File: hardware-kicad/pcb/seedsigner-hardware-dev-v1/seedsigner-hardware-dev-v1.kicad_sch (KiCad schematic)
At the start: 17 parts, among them U1 LuckFox_Pico_MINI, U2 WAVESHARE_LCD_BUTTON_BOARD_1.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

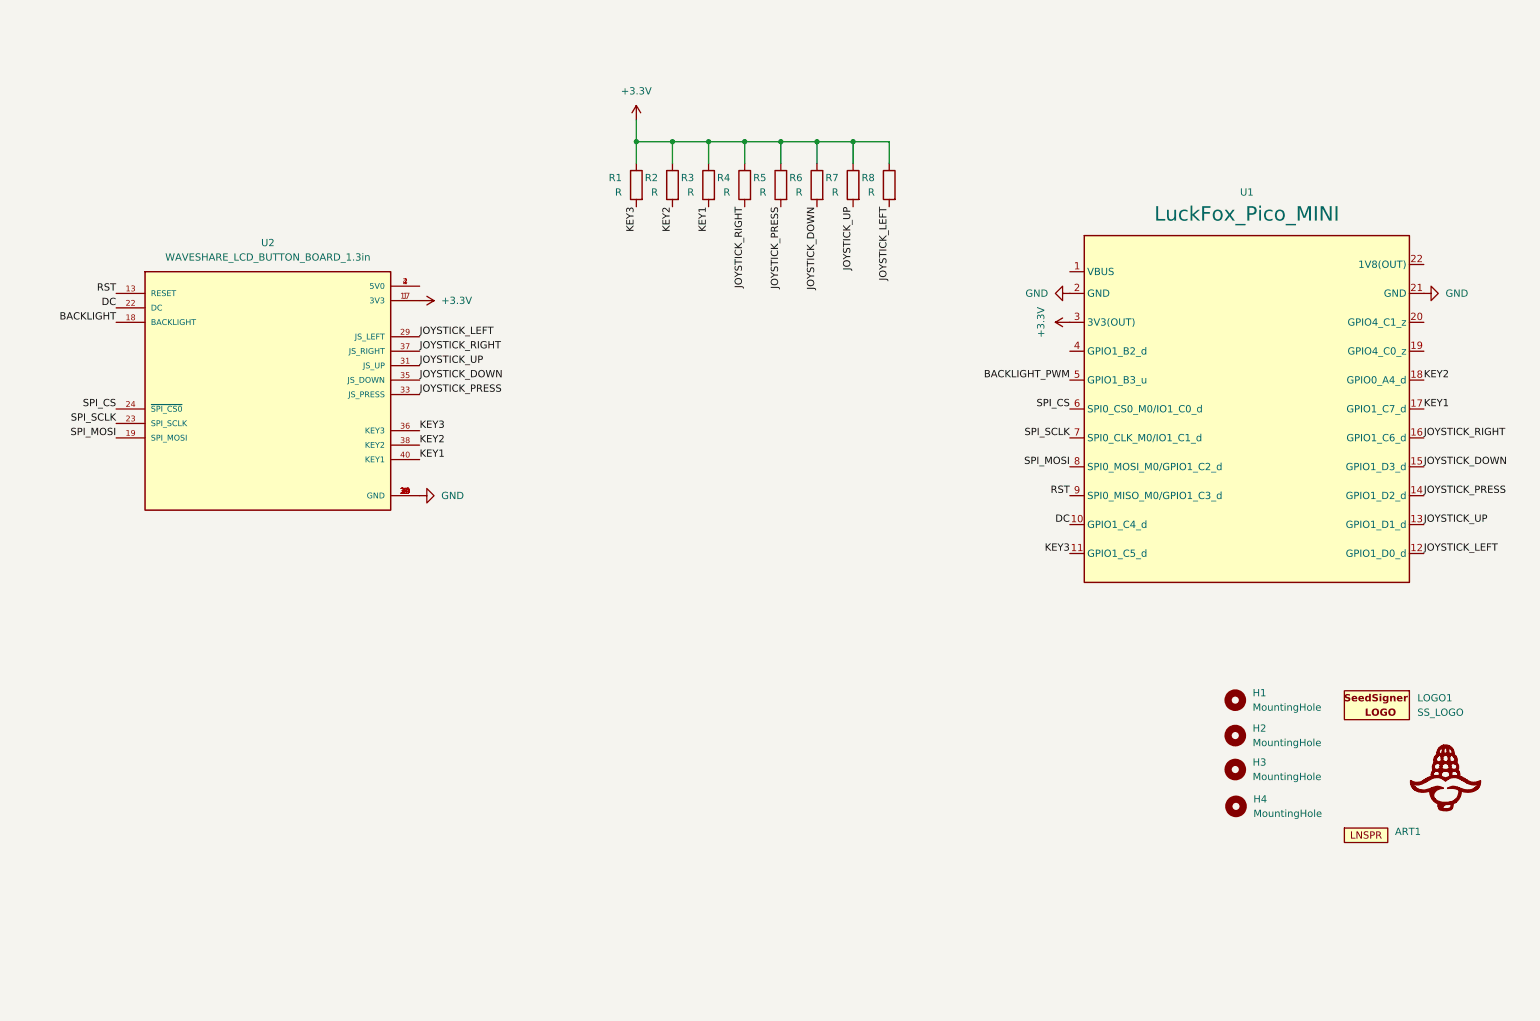
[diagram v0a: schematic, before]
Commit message: seedsigner hardware dev v1 all footprints created and placed
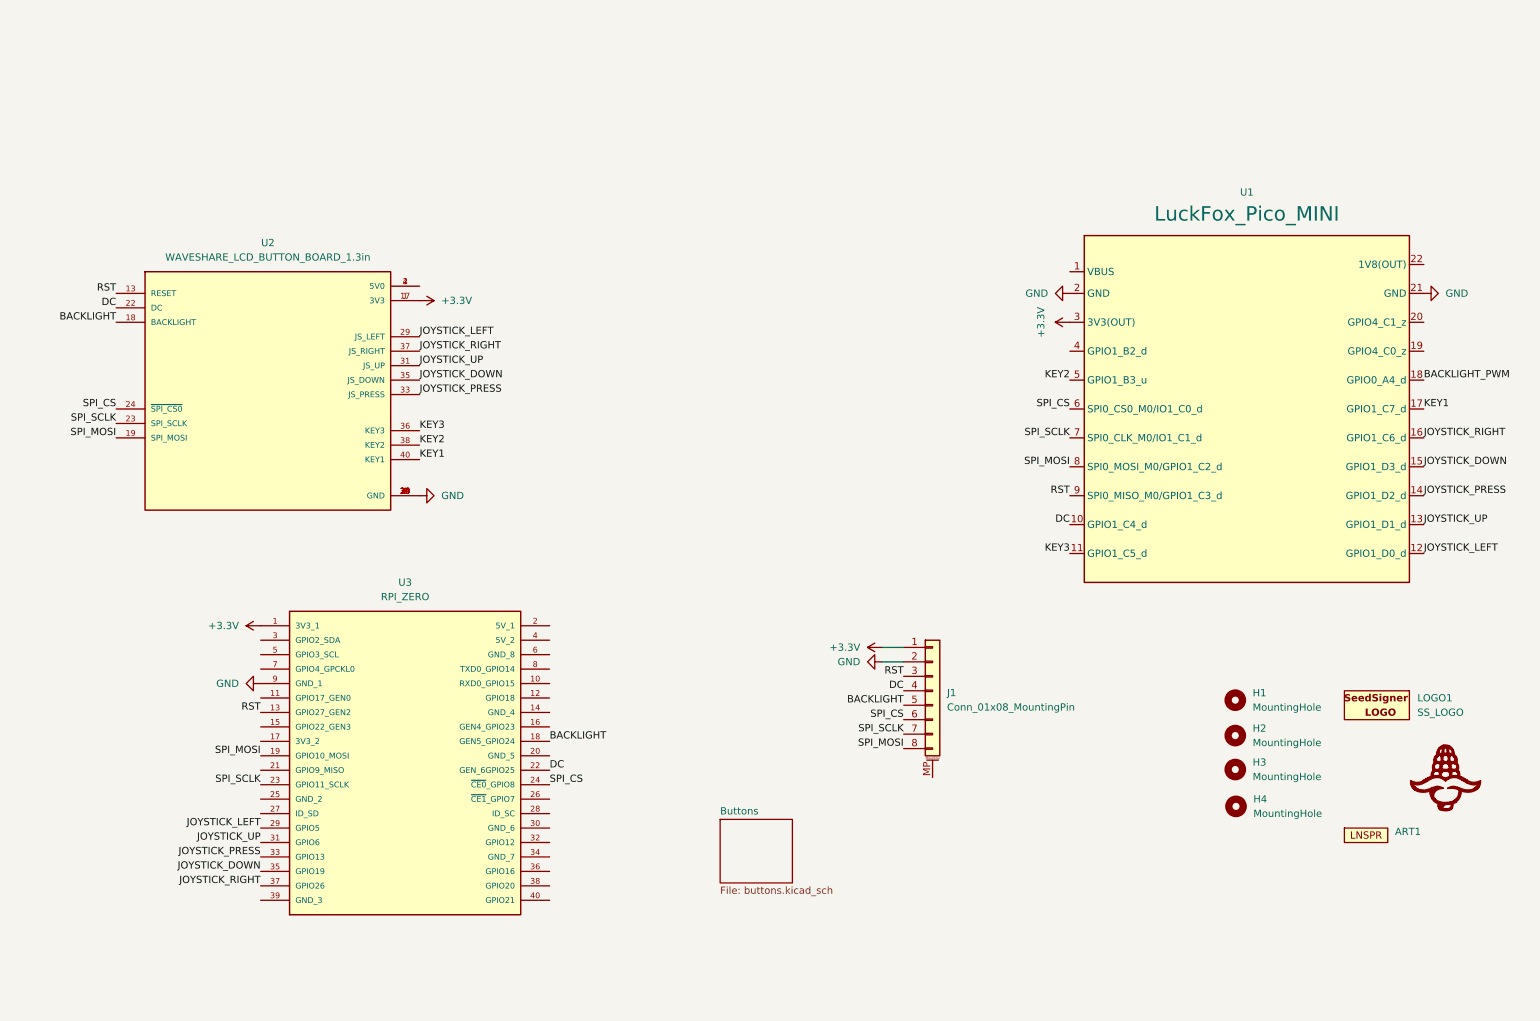
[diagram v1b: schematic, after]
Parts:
- removed R1, R2, R3, R4, R5, R6, R7, R8: R, Resistor_SMD:R_0603_1608Metric_Pad0.98x0.95mm_HandSolder, symbol Device:R
- added J1: Conn_01x08_MountingPin, Connector_PinHeader_2.54mm:PinHeader_1x08_P2.54mm_Horizontal, symbol Connector_Generic_MountingPin:Conn_01x08_MountingPin
- added U3: RPI_ZERO, seedsigner-luckfox:RPi_Zero, symbol SeedSigner:RPI_ZERO
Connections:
- net +3.3V: now also J1.1 (Pin_1), U3.1 (3V3_1)
- net BACKLIGHT: now also J1.5 (Pin_5), U3.18 (GEN5_GPIO24)
- net BACKLIGHT_PWM: now also U1.18 (GPIO0_A4_d); no longer U1.5 (GPIO1_B3_u)
- net DC: now also J1.4 (Pin_4), U3.22 (GEN_6GPIO25)
- net GND: now also J1.2 (Pin_2), U3.9 (GND_1)
- net JOYSTICK_DOWN: now also U3.35 (GPIO19)
- net JOYSTICK_LEFT: now also U3.29 (GPIO5)
- net JOYSTICK_PRESS: now also U3.33 (GPIO13)
- net JOYSTICK_RIGHT: now also U3.37 (GPIO26)
- net JOYSTICK_UP: now also U3.31 (GPIO6)
- net KEY2: now also U1.5 (GPIO1_B3_u); no longer U1.18 (GPIO0_A4_d)
- net RST: now also J1.3 (Pin_3), U3.13 (GPIO27_GEN2)
- net SPI_CS: now also J1.6 (Pin_6), U3.24 (~{CE0}_GPIO8)
- net SPI_MOSI: now also J1.8 (Pin_8), U3.19 (GPIO10_MOSI)
- net SPI_SCLK: now also J1.7 (Pin_7), U3.23 (GPIO11_SCLK)
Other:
- added sheet Buttons (buttons.kicad_sch)

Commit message: use hierarchical sheets in kicad
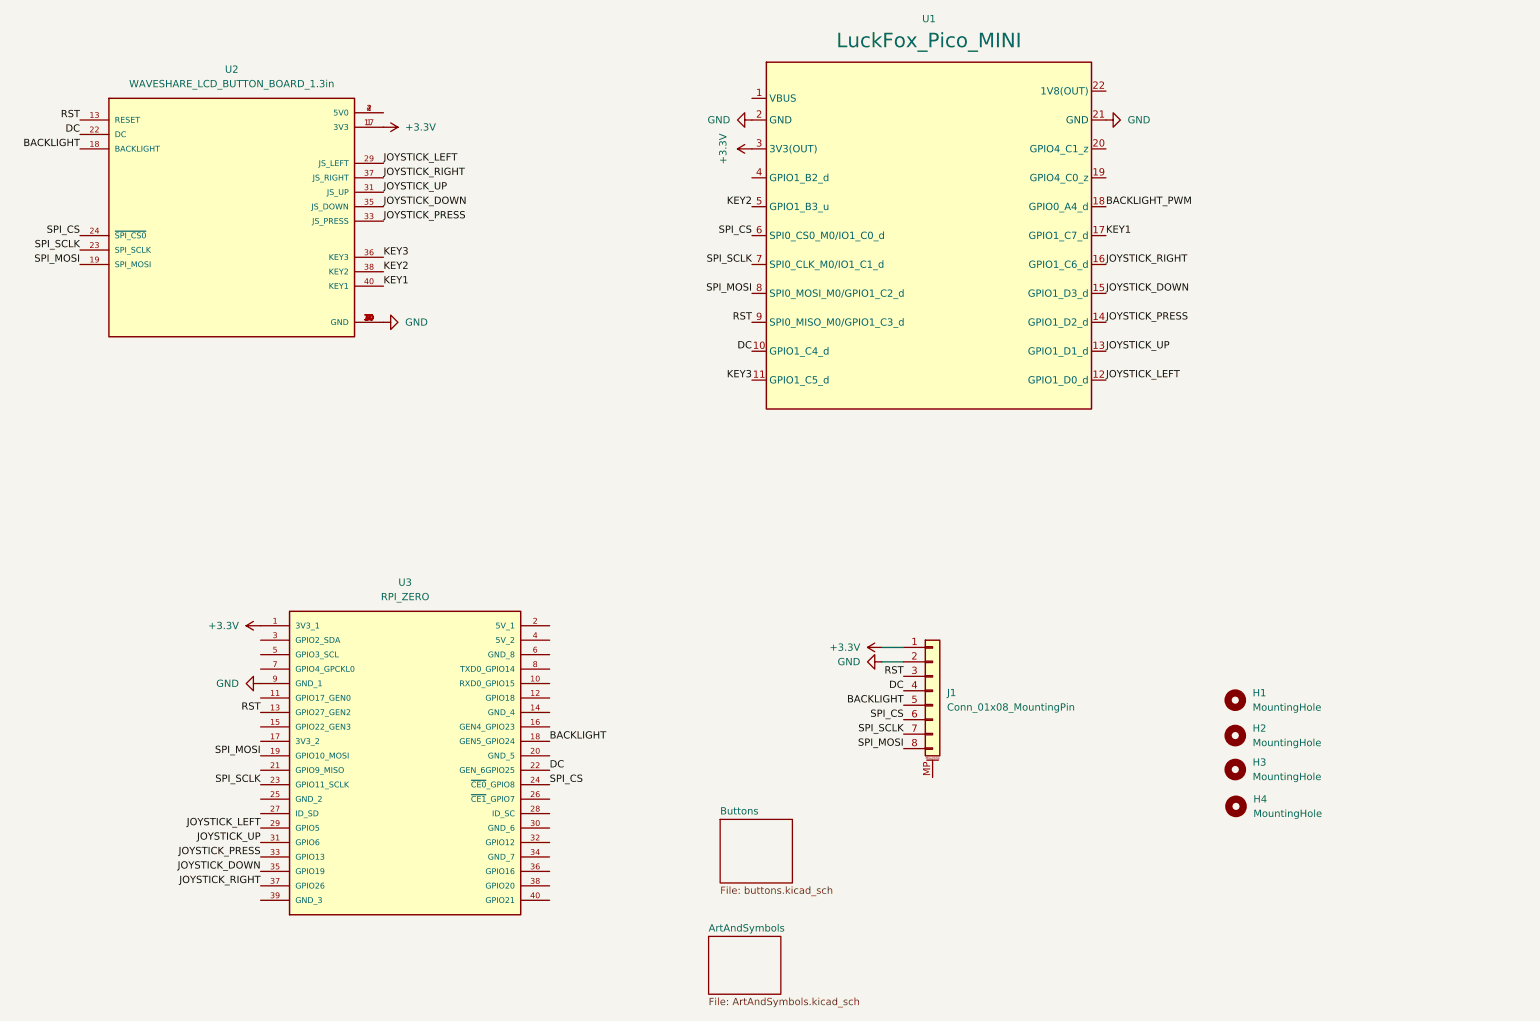
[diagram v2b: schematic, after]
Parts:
- removed ART1: ~, seedsigner-luckfox:LightningSpore_Logo, symbol seedsigner:LIGHTNINGSPORE
- removed LOGO1: SS_LOGO, seedsigner-luckfox:seedsigner-logo-small, symbol SeedSigner:SS_LOGO
- removed LOGO2: CORN-LOGO, seedsigner-luckfox:corn-logo, symbol SeedSigner:CORN-LOGO
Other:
- added sheet ArtAndSymbols (ArtAndSymbols.kicad_sch)
- moved on the sheet: U1, U2

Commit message: update library paths and modularize sch
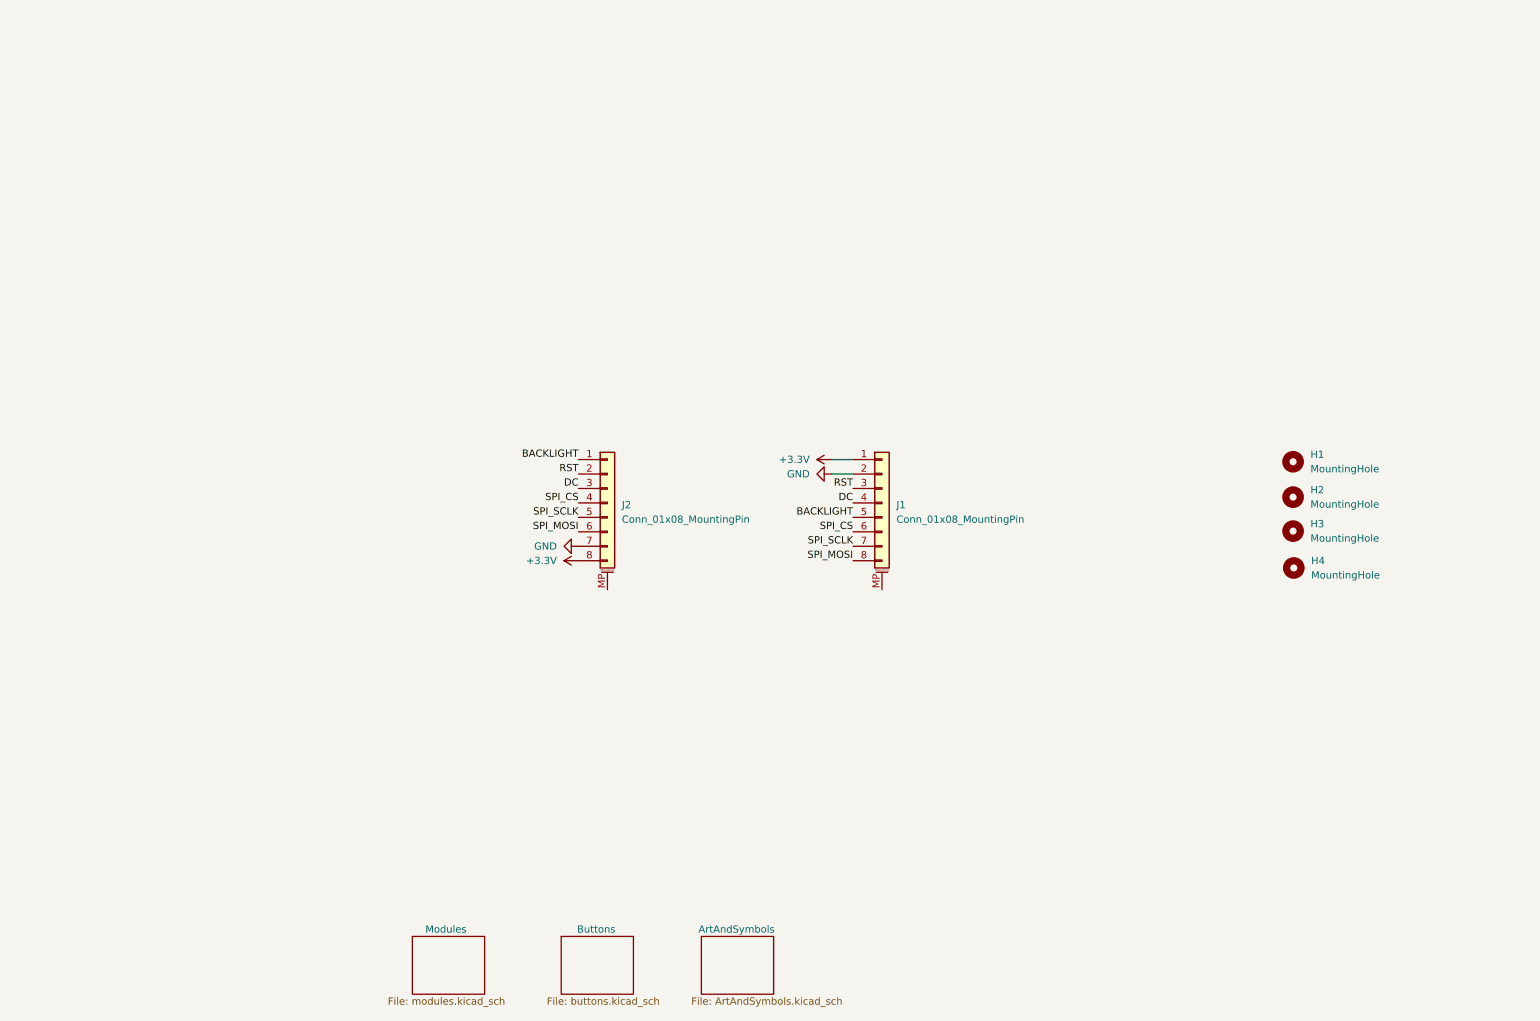
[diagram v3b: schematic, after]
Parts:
- removed U1: LuckFox_Pico_MINI, seedsigner-luckfox:LUCKFOX_PICO_MINI, symbol Luckfox:LuckFox_Pico_MINI
- removed U2: WAVESHARE_LCD_BUTTON_BOARD_1.3in, seedsigner-luckfox:WAVESHARE_LCD_BUTTON, symbol SeedSigner:WAVESHARE_LCD_BUTTON
- removed U3: RPI_ZERO, seedsigner-luckfox:RPi_Zero, symbol SeedSigner:RPI_ZERO
- added J2: Conn_01x08_MountingPin, Connector_PinHeader_2.54mm:PinHeader_1x08_P2.54mm_Horizontal, symbol Connector_Generic_MountingPin:Conn_01x08_MountingPin
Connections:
- net +3.3V: now also J2.8 (Pin_8)
- net BACKLIGHT: now also J2.1 (Pin_1)
- net DC: now also J2.3 (Pin_3)
- net GND: now also J2.7 (Pin_7)
- net RST: now also J2.2 (Pin_2)
- net SPI_CS: now also J2.4 (Pin_4)
- net SPI_MOSI: now also J2.6 (Pin_6)
- net SPI_SCLK: now also J2.5 (Pin_5)
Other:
- added sheet Modules (modules.kicad_sch)
- moved on the sheet: H1, H2, H3, H4, J1

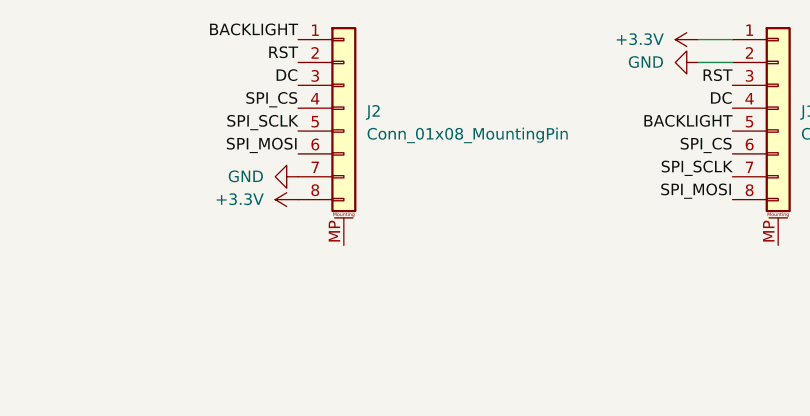
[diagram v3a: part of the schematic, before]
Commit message: autoroute the hardware devboard
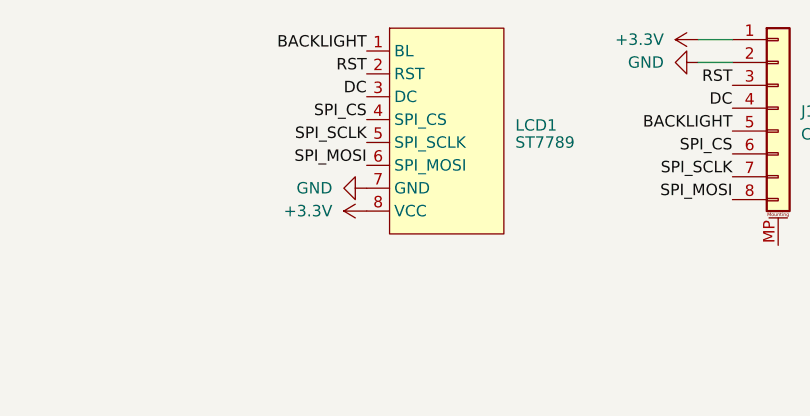
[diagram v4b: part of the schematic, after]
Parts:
- removed J2: Conn_01x08_MountingPin, Connector_PinHeader_2.54mm:PinHeader_1x08_P2.54mm_Horizontal, symbol Connector_Generic_MountingPin:Conn_01x08_MountingPin
- added LCD1: ST7789, Connector_PinHeader_2.54mm:PinHeader_1x08_P2.54mm_Vertical, symbol SeedSigner:LCD_ST7789
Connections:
- net +3.3V: now also LCD1.8 (VCC)
- net BACKLIGHT: now also LCD1.1 (BL)
- net DC: now also LCD1.3 (DC)
- net GND: now also LCD1.7 (GND)
- net RST: now also LCD1.2 (RST)
- net SPI_CS: now also LCD1.4 (SPI_CS)
- net SPI_MOSI: now also LCD1.6 (SPI_MOSI)
- net SPI_SCLK: now also LCD1.5 (SPI_SCLK)
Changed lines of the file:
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@@
 	)
 	(label "SPI_SCLK"
-		(at 116.84 106.68 180)
+		(at 124.46 107.95 180)
 		(effects
 			(font
@@
 	)
 	(label "SPI_CS"
-		(at 116.84 104.14 180)
+		(at 124.46 105.41 180)
 		(effects
 			(font
@@
 	)
 	(label "BACKLIGHT"
-		(at 116.84 96.52 180)
+		(at 124.46 97.79 180)
 		(effects
 			(font
@@
 	)
 	(label "SPI_MOSI"
-		(at 116.84 109.22 180)
+		(at 124.46 110.49 180)
 		(effects
 			(font
@@
 	)
 	(label "DC"
-		(at 116.84 101.6 180)
+		(at 124.46 102.87 180)
 		(effects
 			(font
@@
 	)
 	(label "RST"
-		(at 116.84 99.06 180)
+		(at 124.46 100.33 180)
 		(effects
 			(font
@@
 	)
 	(symbol
+		(lib_id "SeedSigner:LCD_ST7789")
+		(at 133.35 106.68 0)
+		(unit 1)
+		(exclude_from_sim no)
+		(in_bom yes)
+		(on_board yes)
+		(dnp no)
+		(fields_autoplaced yes)
+		(property "Reference" "LCD1"
+			(at 140.97 106.0449 0)
+			(effects
+				(font
+					(size 1.27 1.27)
+				)
+				(justify left)
+			)
+		)
+		(property "Value" "ST7789"
+			(at 140.97 107.95 0)
+			(effects
+				(font
+					(size 1.27 1.27)
+				)
+				(justify left)
+			)
+		)
+		(property "Footprint" "Connector_PinHeader_2.54mm:PinHeader_1x08_P2.54mm_Vertical"
+			(at 133.35 106.68 0)
+			(effects
+				(font
+					(size 1.27 1.27)
+				)
+				(hide yes)
+			)
+		)
+		(property "Datasheet" ""
+			(at 133.35 106.68 0)
+			(effects
+				(font
+					(size 1.27 1.27)
+				)
+				(hide yes)
+			)
+		)
+		(property "Description" ""
+			(at 133.35 106.68 0)
+			(effects
+				(font
+					(size 1.27 1.27)
+				)
+				(hide yes)
+			)
+		)
+		(pin "1"
+		)
+		(pin "2"
+		)
+		(pin "3"
+		)
+		(pin "4"
+		)
+		(pin "5"
+		)
+		(pin "6"
+		)
+		(pin "7"
+		)
+		(pin "8"
+		)
+		(instances
+			(project ""
+				(path "/80ddcc25-987b-44b8-ab4f-432d39ad0241"
+					(reference "LCD1")
+					(unit 1)
+				)
+			)
+		)
+	)
+	(symbol
 		(lib_id "Mechanical:MountingHole")
 		(at 242.443 103.124 0)
@@
 	)
 	(symbol
-		(lib_id "Connector_Generic_MountingPin:Conn_01x08_MountingPin")
-		(at 121.92 104.14 0)
-		(unit 1)
-		(exclude_from_sim no)
-		(in_bom yes)
-		(on_board yes)
-		(dnp no)
-		(fields_autoplaced yes)
-		(property "Reference" "J2"
-			(at 124.46 104.4955 0)
-			(effects
-				(font
-					(size 1.27 1.27)
-				)
-				(justify left)
-			)
-		)
-		(property "Value" "Conn_01x08_MountingPin"
-			(at 124.46 107.0355 0)
-			(effects
-				(font
-					(size 1.27 1.27)
-				)
-				(justify left)
-			)
-		)
-		(property "Footprint" "Connector_PinHeader_2.54mm:PinHeader_1x08_P2.54mm_Horizontal"
-			(at 121.92 104.14 0)
-			(effects
-				(font
-					(size 1.27 1.27)
-				)
-				(hide yes)
-			)
-		)
-		(property "Datasheet" "~"
-			(at 121.92 104.14 0)
-			(effects
-				(font
-					(size 1.27 1.27)
-				)
-				(hide yes)
-			)
-		)
-		(property "Description" "Generic connectable mounting pin connector, single row, 01x08, script generated (kicad-library-utils/schlib/autogen/connector/)"
-			(at 121.92 104.14 0)
-			(effects
-				(font
-					(size 1.27 1.27)
-				)
-				(hide yes)
-			)
-		)
-		(pin "MP"
-		)
-		(pin "1"
-		)
-		(pin "6"
-		)
-		(pin "7"
-		)
-		(pin "2"
-		)
-		(pin "3"
-		)
-		(pin "5"
-		)
-		(pin "8"
-		)
-		(pin "4"
-		)
-		(instances
-			(project "seedsigner-hardware-dev-v1"
-				(path "/80ddcc25-987b-44b8-ab4f-432d39ad0241"
-					(reference "J2")
-					(unit 1)
-				)
-			)
-		)
-	)
-	(symbol
 		(lib_id "Mechanical:MountingHole")
 		(at 242.443 96.901 0)
@@
 	(symbol
 		(lib_id "power:GND")
-		(at 116.84 111.76 270)
+		(at 124.46 113.03 270)
 		(unit 1)
 		(exclude_from_sim no)
@@
 		(fields_autoplaced yes)
 		(property "Reference" "#PWR02"
-			(at 110.49 111.76 0)
+			(at 118.11 113.03 0)
 			(effects
 				(font
@@
 		)
 		(property "Value" "GND"
-			(at 113.03 111.7599 90)
+			(at 120.65 113.0299 90)
 			(effects
 				(font
@@
 		)
 		(property "Footprint" ""
-			(at 116.84 111.76 0)
+			(at 124.46 113.03 0)
 			(effects
 				(font
@@
 		)
 		(property "Datasheet" ""
-			(at 116.84 111.76 0)
-			(effects
-				(font
-					(size 1.27 1.27)
-				)
-				(hide yes)
-			)
-		)
-		(property "Description" ""
-			(at 116.84 111.76 0)
+			(at 124.46 113.03 0)
+			(effects
+				(font
+					(size 1.27 1.27)
+				)
+				(hide yes)
+			)
+		)
+		(property "Description" ""
+			(at 124.46 113.03 0)
 			(effects
 				(font
@@
 	(symbol
 		(lib_id "power:+3.3V")
-		(at 116.84 114.3 90)
+		(at 124.46 115.57 90)
 		(unit 1)
 		(exclude_from_sim no)
@@
 		(fields_autoplaced yes)
 		(property "Reference" "#PWR01"
-			(at 120.65 114.3 0)
+			(at 128.27 115.57 0)
 			(effects
 				(font
@@
 		)
 		(property "Value" "+3.3V"
-			(at 113.03 114.2999 90)
+			(at 120.65 115.5699 90)
 			(effects
 				(font
@@
 		)
 		(property "Footprint" ""
-			(at 116.84 114.3 0)
+			(at 124.46 115.57 0)
 			(effects
 				(font
@@
 		)
 		(property "Datasheet" ""
-			(at 116.84 114.3 0)
-			(effects
-				(font
-					(size 1.27 1.27)
-				)
-				(hide yes)
-			)
-		)
-		(property "Description" ""
-			(at 116.84 114.3 0)
-			(effects
-				(font
+			(at 124.46 115.57 0)
+			(effects
+				(font
+					(size 1.27 1.27)
+				)
+				(hide yes)
+			)
+		)
+		(property "Description" ""
+			(at 124.46 115.57 0)
+			(effects
+				(font
